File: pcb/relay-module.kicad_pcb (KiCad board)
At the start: 2 copper layers, 50 x 50 mm, 37 parts, among them J1 AVR-UPDI-6, K1 PR24-5V-900-1A, P1 MountingHole_Pad, P2 MountingHole_Pad, P3 MountingHole_Pad, P4 MountingHole_Pad, Q1 MMBT3904, U2 ATtiny1616-M, U3 LTV-356T, U4 TPS61023DRLR

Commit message: initial checkin
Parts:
- removed C4, C5, C6: 10uF, Capacitor_SMD:C_0603_1608Metric
- removed L2: 1uH, Inductor_SMD:L_Wuerth_MAPI-2010
- removed R5: 100K, Resistor_SMD:R_0603_1608Metric
- removed R6: 732K, Resistor_SMD:R_0603_1608Metric
- removed U4: TPS61023DRLR, CRGM Power:SOTFL50P160X60-6N
- added J3: Power, Connector_JST:JST_SH_SM04B-SRSS-TB_1x04-1MP_P1.00mm_Horizontal, F.Cu at (63.3, 161.7)
- added S1: ~, CRGM Symbols:HIGH-VOLTAGE-5MM, F.Cu at (96.1, 133.7)
- added S2: ~, CRGM Symbols:HIGH-VOLTAGE-5MM, F.Cu at (53.9, 134.0)
- added kibuzzard-67E37192: G***, kibuzzard-67E37192, F.Cu at (53.9, 124.0)
- added kibuzzard-67E371A7: G***, kibuzzard-67E371A7, F.Cu at (96.0, 124.0)
- added kibuzzard-67E3720C: G***, kibuzzard-67E3720C, F.Cu at (54.0, 144.0)
- added kibuzzard-67E3720C: G***, kibuzzard-67E3720C, F.Cu at (96.0, 144.0)
- J2: value ~ -> QWICC; footprint Connector_JST:JST_SH_BM04B-SRSS-TB_1x04-1MP_P1.00mm_Vertical -> Connector_JST:JST_SH_SM04B-SRSS-TB_1x04-1MP_P1.00mm_Horizontal
- moved FID2 56.0 mm to (97.0, 156.0)
- moved J1 41.7 mm to (97.0, 153.0)
- moved D1 35.5 mm to (75.6, 155.8)
- moved J2 33.9 mm to (87.1, 161.7), turned to 0 degrees
- moved R4 32.5 mm to (87.2, 156.9), turned to 90 degrees
- moved R3 30.4 mm to (88.7, 156.9), turned to 90 degrees
- moved C1 29.0 mm to (78.1, 155.3), turned to 90 degrees
- moved Q1 21.2 mm to (75.3, 158.6), turned to 0 degrees
- moved JP1 17.7 mm to (87.8, 154.1), turned to 180 degrees
- moved U2 14.2 mm to (80.9, 155.1)
- moved R2 10.6 mm to (72.5, 158.6), turned to 90 degrees
- moved FID3 10.3 mm to (91.5, 117.0)
- moved U3 8.98 mm to (72.8, 162.5), turned to 180 degrees
- moved R1 4.52 mm to (78.1, 163.0)
- moved K1 4.00 mm to (72.0, 131.0)
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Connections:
- net /I2C Interface/RELAY_CTRL renamed /RELAY_CTRL
- net /I2C Interface/SCL renamed /SCL
- net /I2C Interface/SDA renamed /SDA
- net /I2C Interface/UPDI renamed /UPDI
- net /Relay/LOAD_IN renamed /LOAD_IN
- net /Relay/LOAD_OUT renamed /LOAD_OUT
- net /Relay/NEUTRAL renamed /NEUTRAL
- net /Relay/RELAY_GND renamed /RELAY_CONTROL
- U3 pad 4: +5V -> +3.3V
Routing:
- net +5V: track 0.00 -> 31.9 mm
- net /RELAY_CONTROL: track 0.00 -> 23.1 mm, vias 0 -> 1
- net /UPDI: track 0.00 -> 18.5 mm, vias 0 -> 1
- net /RELAY_CTRL: track 0.00 -> 11.8 mm, vias 0 -> 2
- net /SCL: track 0.00 -> 9.65 mm
- net /SDA: track 0.00 -> 8.08 mm
- net +3.3V: track 0.00 -> 7.90 mm, vias 0 -> 5
- net GND: track 0.00 -> 6.61 mm, vias 0 -> 66
- net Net-(R2-Pad1): track 0.00 -> 3.95 mm
- net Net-(R1-Pad2): track 0.00 -> 2.35 mm
- net Net-(JP1-B): track 0.00 -> 2.26 mm
- net Net-(JP1-A): track 0.00 -> 2.14 mm
- net Net-(Q1-B): track 0.00 -> 1.92 mm
- added copper zone on In1.Cu, net +3.3V
- added copper zone on B.Cu, net /LOAD_IN
- added copper zone on B.Cu, net /LOAD_OUT
- added copper zone on B.Cu, net /NEUTRAL
- added copper zone on F.Cu, net GND
- added copper zone on In2.Cu, net GND
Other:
- copper layers 2 -> 4
- rule pad_to_mask_clearance: 0 -> 0.038

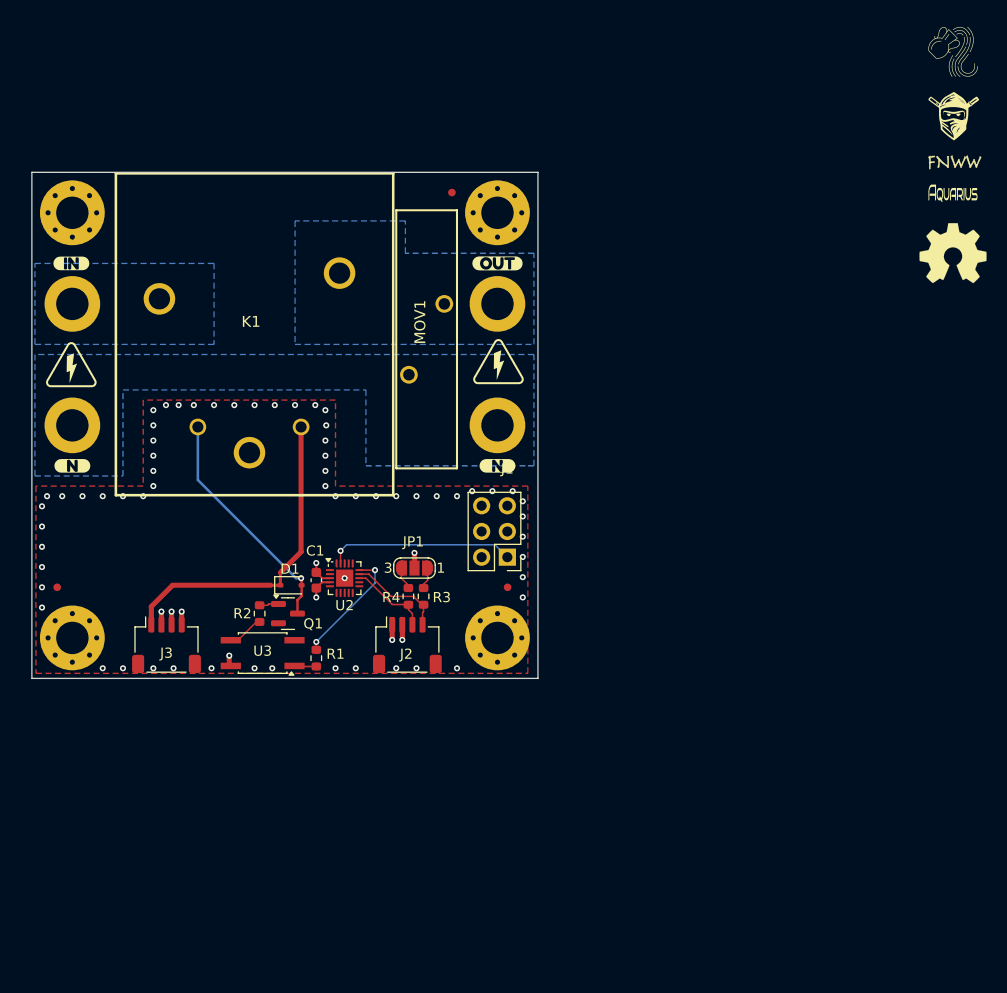
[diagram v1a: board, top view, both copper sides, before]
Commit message: Updated silkscreen
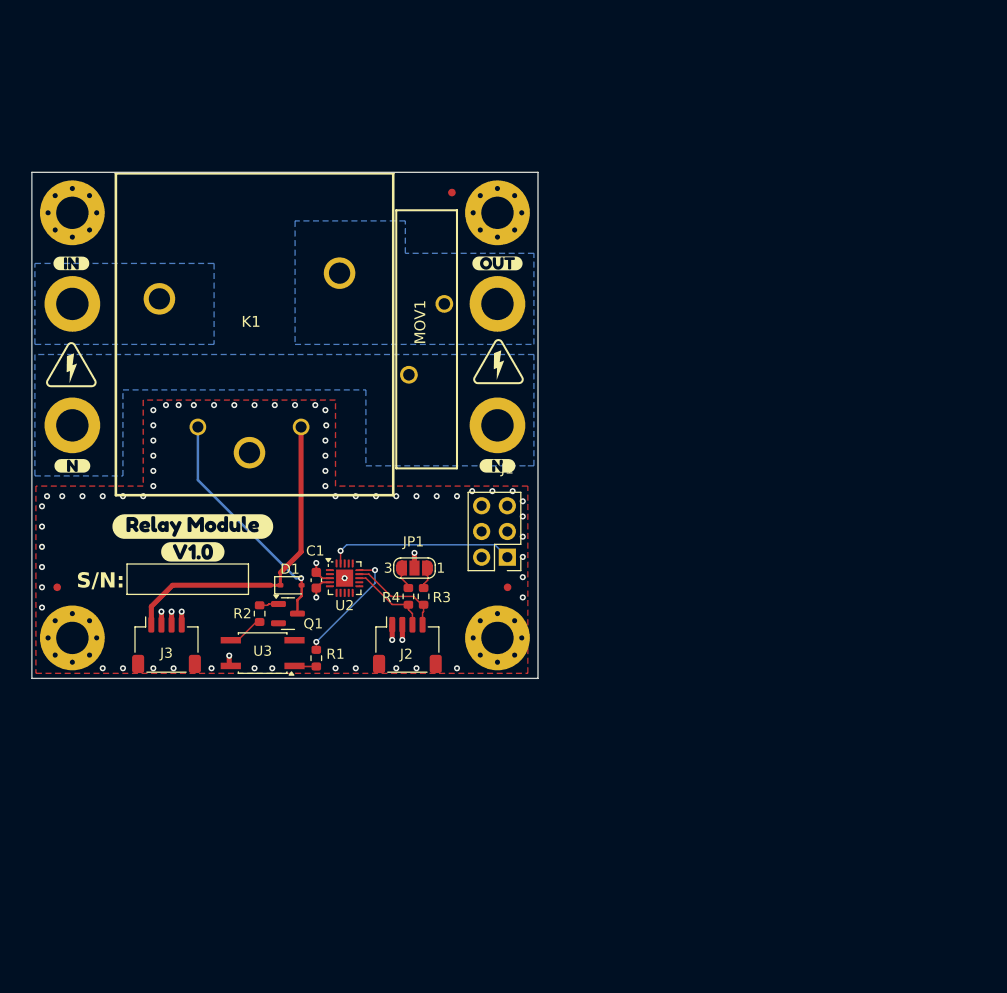
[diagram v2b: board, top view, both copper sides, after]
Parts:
- removed LOGO2: ~, CRGM Logos:Aquarius Name 2mmx5mm
- removed LOGO4: ~, CRGM Logos:FNWW Name 2mmx5mm
- added S3: ~, CRGM Symbols:HIGH-VOLTAGE-5MM, B.Cu at (96.1, 133.7)
- added S4: ~, CRGM Symbols:HIGH-VOLTAGE-5MM, B.Cu at (53.9, 134.0)
- added kibuzzard-67F88791: G***, kibuzzard-67F88791, B.Cu at (70.2, 162.2)
- added kibuzzard-67F88799: G***, kibuzzard-67F88799, B.Cu at (69.8, 158.3)
- added kibuzzard-67F8886E: G***, kibuzzard-67F8886E, F.Cu at (65.9, 150.0)
- added kibuzzard-67F88877: G***, kibuzzard-67F88877, F.Cu at (65.9, 152.5)
- added kibuzzard-67F88910: G***, kibuzzard-67F88910, B.Cu at (91.6, 136.3)
- added kibuzzard-67F88910: G***, kibuzzard-67F88910, B.Cu at (58.9, 133.9)
- LOGO1: footprint CRGM Logos:Aquarius Logo 5mm -> CRGM Logos:Aquarius Logo 10mm; moved to B.Cu
- LOGO3: footprint CRGM Logos:FNWW Face 5mm -> CRGM Logos:FNWW Face 10mm; moved to B.Cu
- LOGO5: footprint Symbol:OSHW-Symbol_6.7x6mm_SilkScreen -> Symbol:OSHW-Logo_5.7x6mm_SilkScreen; moved to B.Cu
- moved LOGO1 89.9 mm to (64.9, 153.8), turned to 180 degrees
- moved LOGO3 76.5 mm to (76.9, 153.9), turned to 180 degrees
- moved LOGO5 65.4 mm to (86.5, 159.2), turned to 180 degrees
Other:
- board text added: "Aquarius"
- board text added: "FNWW"
- board text added: "S/N:"

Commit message: v1.0 Relay Module Panel 2x2
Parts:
- removed FID1, FID2, FID3: Fiducial, Fiducial:Fiducial_0.75mm_Mask1.5mm
- removed kibuzzard-67F88791: G***, kibuzzard-67F88791
- removed kibuzzard-67F88799: G***, kibuzzard-67F88799
- removed kibuzzard-67F8886E: G***, kibuzzard-67F8886E
- removed kibuzzard-67F88877: G***, kibuzzard-67F88877
- added C2: .1uF, Capacitor_SMD:C_0603_1608Metric, F.Cu at (60.0, 141.2)
- added J4: Power Out, CRGM Connector:SM04B-SRSS-TB, F.Cu at (62.2, 144.3)
- added kibuzzard-6801052A: G***, kibuzzard-6801052A, F.Cu at (91.6, 133.6)
- added kibuzzard-6801053F: G***, kibuzzard-6801053F, F.Cu at (91.6, 135.8)
- added kibuzzard-6801AC5F: G***, kibuzzard-6801AC5F, F.Cu at (76.3, 136.2)
- added kibuzzard-6801ACAF: G***, kibuzzard-6801ACAF, F.Cu at (76.4, 138.7)
- added kibuzzard-6802999E: G***, kibuzzard-6802999E, B.Cu at (75.0, 120.8)
- added kibuzzard-68029C11: G***, kibuzzard-68029C11, B.Cu at (75.0, 117.6)
- J2: footprint Connector_JST:JST_SH_SM04B-SRSS-TB_1x04-1MP_P1.00mm_Horizontal -> CRGM Connector:SM04B-SRSS-TB
- J3: value Power -> Power In; footprint Connector_JST:JST_SH_SM04B-SRSS-TB_1x04-1MP_P1.00mm_Horizontal -> CRGM Connector:SM04B-SRSS-TB
- LOGO1: footprint CRGM Logos:Aquarius Logo 10mm -> CRGM Logos:Aquarius Logo 5mm
- LOGO3: footprint CRGM Logos:FNWW Face 10mm -> CRGM Logos:FNWW Face 5mm
- U2: footprint Package_DFN_QFN:VQFN-20-1EP_3x3mm_P0.4mm_EP1.7x1.7mm -> CRG Makes:VQFN-20-1EP_3x3mm_P0.4mm_EP1.7x1.7mm_ThermalVias
- moved J1 41.9 mm to (58.9, 135.5), turned to -90 degrees
- moved LOGO1 41.9 mm to (75.1, 113.2)
- moved J3 30.0 mm to (87.8, 144.3), turned to 180 degrees
- moved U3 24.8 mm to (73.2, 137.7), turned to 90 degrees
- moved Q1 24.7 mm to (67.4, 135.2), turned to -90 degrees
- moved R1 24.4 mm to (70.1, 140.0)
- moved R2 23.9 mm to (69.9, 134.8), turned to -90 degrees
- moved D1 23.4 mm to (64.3, 135.3), turned to -90 degrees
- moved LOGO5 22.1 mm to (70.2, 144.2)
- moved C1 21.9 mm to (62.7, 139.7)
- moved U2 21.9 mm to (65.6, 139.5)
- moved J2 21.2 mm to (75.0, 144.3), turned to 180 degrees
- moved JP1 19.1 mm to (78.5, 137.4), turned to -90 degrees
- moved R4 18.5 mm to (78.6, 140.5), turned to 180 degrees
- moved R3 18.0 mm to (78.6, 142.0), turned to 180 degrees
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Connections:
- net /RELAY_CTRL renamed RELAY_CTRL
- net /UPDI renamed UPDI
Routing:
- net +5V: track 31.9 -> 62.5 mm
- net /SDA: track 8.08 -> 21.3 mm
- net UPDI: track 18.5 -> 7.89 mm
- net /SCL: track 9.65 -> 18.4 mm
- net /RELAY_CONTROL: track 23.1 -> 14.5 mm, vias 1 -> 0
- net RELAY_CTRL: track 11.8 -> 3.28 mm, vias 2 -> 0
- net Net-(JP1-A): track 2.14 -> 7.75 mm
- net Net-(R2-Pad1): track 3.95 -> 7.29 mm
- net GND: track 6.61 -> 3.98 mm, vias 66 -> 63
- net +3.3V: track 7.90 -> 10.2 mm, vias 5 -> 7
- net Net-(R1-Pad2): track 2.35 -> 1.84 mm
- net /NEUTRAL: vias 0 -> 68
- net /LOAD_OUT: vias 0 -> 56
- net /LOAD_IN: vias 0 -> 52
- added copper zone on F.Cu, net /LOAD_IN
- added copper zone on In1.Cu, net /LOAD_IN
- added copper zone on In2.Cu, net /LOAD_IN
- added copper zone on F.Cu, net /LOAD_OUT
- added copper zone on In1.Cu, net /LOAD_OUT
- added copper zone on In2.Cu, net /LOAD_OUT
- added copper zone on F.Cu, net /NEUTRAL
- added copper zone on In1.Cu, net /NEUTRAL
- added copper zone on In2.Cu, net /NEUTRAL
- added copper zone on B.Cu, net GND
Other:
- board text added: "MCU"
- board text added: "POWER"
- board text added: "Score Line"

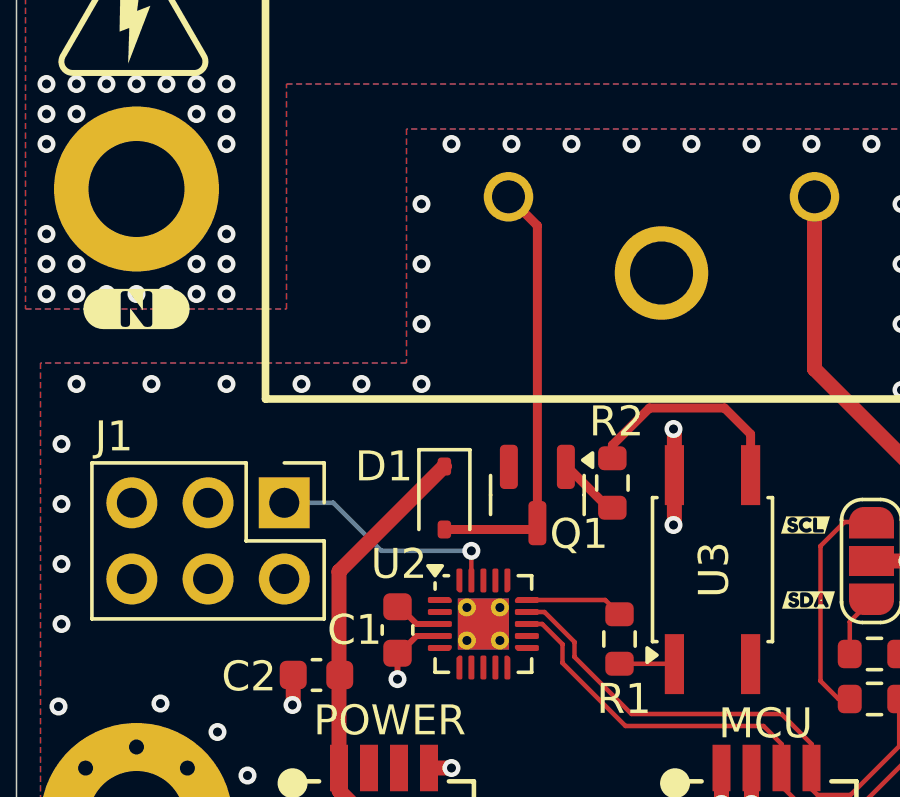
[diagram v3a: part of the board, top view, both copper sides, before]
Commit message: Updated for panelization.
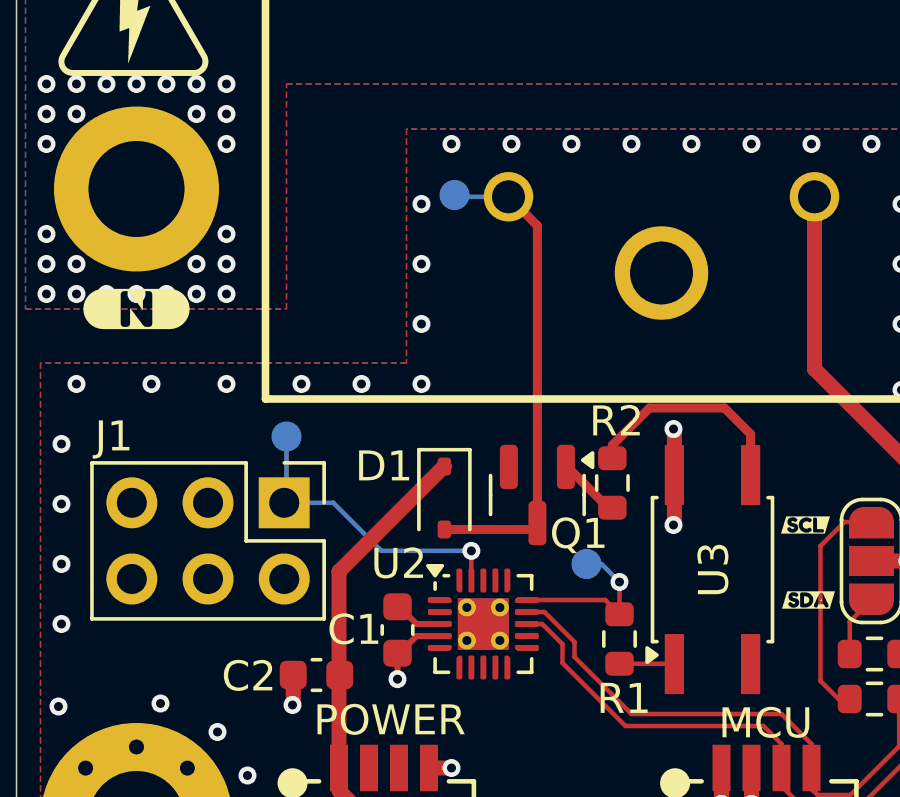
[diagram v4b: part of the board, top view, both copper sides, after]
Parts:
- added TP1: RELAY_CONTROL, TestPoint:TestPoint_Pad_D1.0mm, B.Cu at (64.6, 125.2)
- added TP2: RELAY_CTRL, TestPoint:TestPoint_Pad_D1.0mm, B.Cu at (69.0, 137.5)
- added TP3: UPDI, TestPoint:TestPoint_Pad_D1.0mm, B.Cu at (59.0, 133.2)
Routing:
- net RELAY_CTRL: track 3.28 -> 5.71 mm, vias 0 -> 1
- net UPDI: track 7.89 -> 10.1 mm
- net /RELAY_CONTROL: track 14.5 -> 16.3 mm

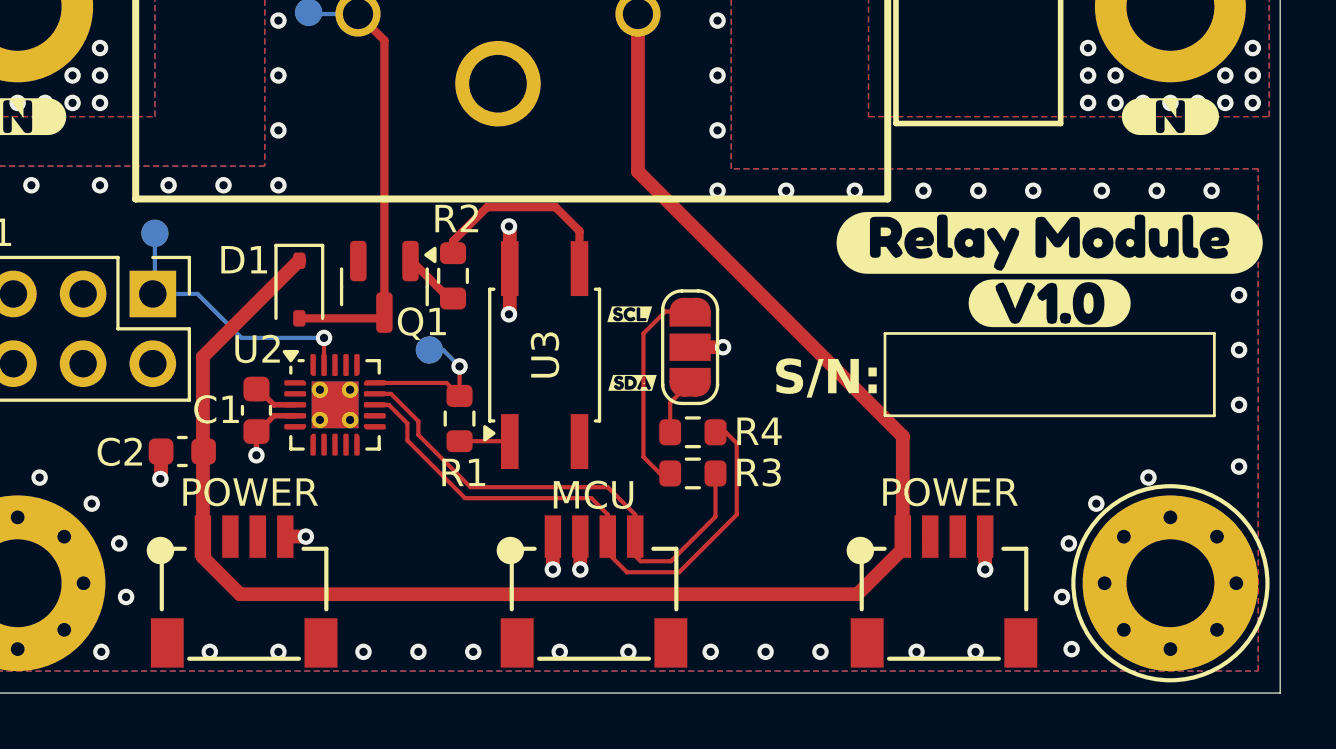
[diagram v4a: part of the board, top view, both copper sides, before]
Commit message: Added power, relay LEDs
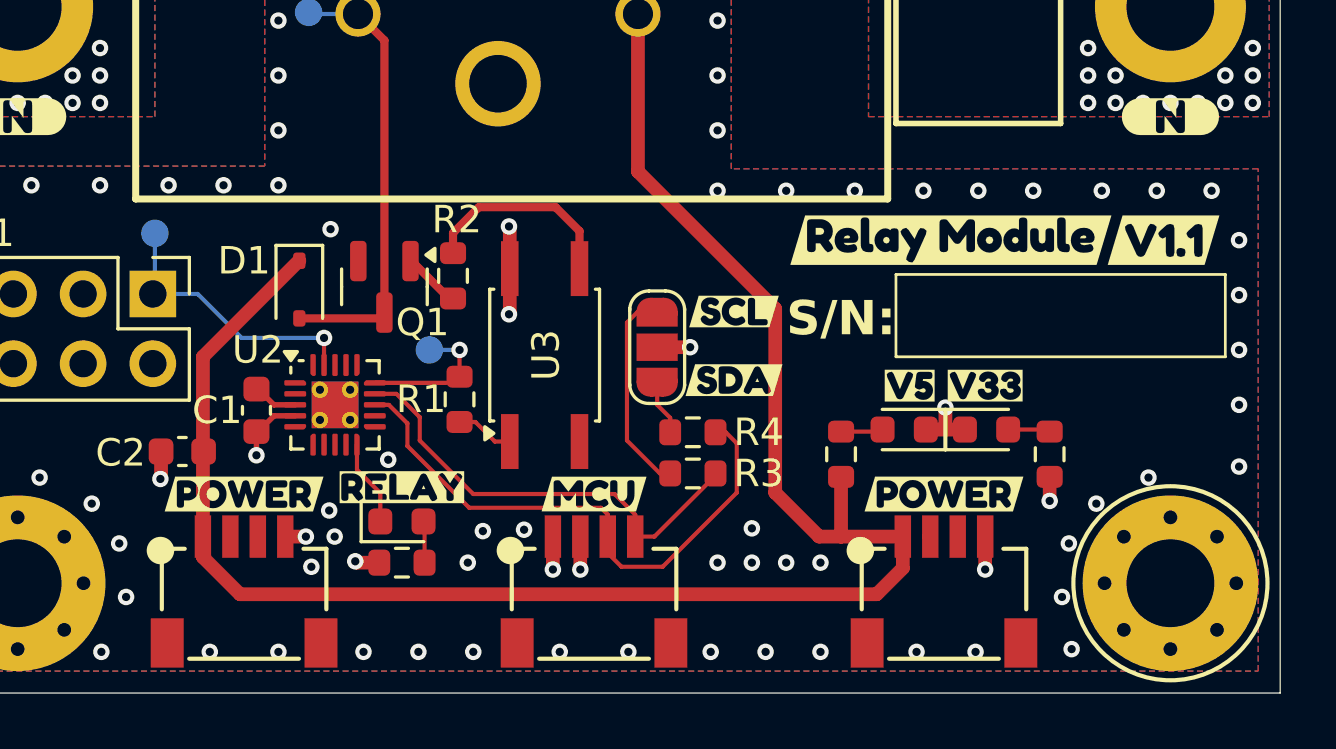
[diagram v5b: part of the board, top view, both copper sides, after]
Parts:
- removed kibuzzard-6801052A: G***, kibuzzard-6801052A
- removed kibuzzard-6801053F: G***, kibuzzard-6801053F
- removed kibuzzard-6801AC5F: G***, kibuzzard-6801AC5F
- removed kibuzzard-6801ACAF: G***, kibuzzard-6801ACAF
- added D3: Blue, LED_SMD:LED_0603_1608Metric, F.Cu at (86.3, 140.4)
- added D4: Blue, LED_SMD:LED_0603_1608Metric, F.Cu at (89.3, 140.4)
- added D5: Red, LED_SMD:LED_0603_1608Metric, F.Cu at (68.0, 143.8)
- added R5: 4.7k, Resistor_SMD:R_0603_1608Metric, F.Cu at (84.0, 141.3)
- added R6: 1k, Resistor_SMD:R_0603_1608Metric, F.Cu at (91.6, 141.3)
- added R7: 1k, Resistor_SMD:R_0603_1608Metric, F.Cu at (68.0, 145.2)
- added kibuzzard-68226E29: G***, kibuzzard-68226E29, F.Cu at (80.1, 136.1)
- added kibuzzard-68226E38: G***, kibuzzard-68226E38, F.Cu at (80.1, 138.6)
- added kibuzzard-682275E1: G***, kibuzzard-682275E1, F.Cu at (68.0, 142.5)
- added kibuzzard-6822763A: G***, kibuzzard-6822763A, F.Cu at (86.5, 138.8)
- added kibuzzard-68227650: G***, kibuzzard-68227650, F.Cu at (89.2, 138.8)
- added kibuzzard-6822769A: G***, kibuzzard-6822769A, F.Cu at (88.0, 133.5)
- added kibuzzard-68227700: G***, kibuzzard-68227700, F.Cu at (95.8, 133.5)
- added kibuzzard-682277DB: G***, kibuzzard-682277DB, F.Cu at (62.2, 142.8)
- added kibuzzard-682277DB: G***, kibuzzard-682277DB, F.Cu at (87.8, 142.8)
- added kibuzzard-682277F7: G***, kibuzzard-682277F7, F.Cu at (75.0, 142.8)
- moved JP1 1.20 mm to (77.3, 137.4)
- moved R1 0.70 mm to (70.1, 139.3)
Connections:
- U2 pad 10: unconnected-(U2-PB4-Pad10) -> RELAY_LED
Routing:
- net +5V: track 62.5 -> 66.9 mm
- net RELAY_LED: track 0.00 -> 3.15 mm
- net GND: track 3.98 -> 6.21 mm, vias 63 -> 77
- net /SCL: track 18.4 -> 16.5 mm
- net +3.3V: track 10.2 -> 12.0 mm, vias 7 -> 9
- net /V5LED: track 0.00 -> 1.54 mm
- net /V3.3LED: track 0.00 -> 1.54 mm
- net Net-(D5-A): track 0.00 -> 1.52 mm
- net RELAY_CTRL: track 5.71 -> 4.69 mm
- net /SDA: track 21.3 -> 20.8 mm
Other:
- board text removed: "MCU"
- board text removed: "POWER"
- board text removed: "Score Line"
